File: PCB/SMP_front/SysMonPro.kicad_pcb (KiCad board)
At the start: 2 copper layers, 100 x 100 mm, 0 parts

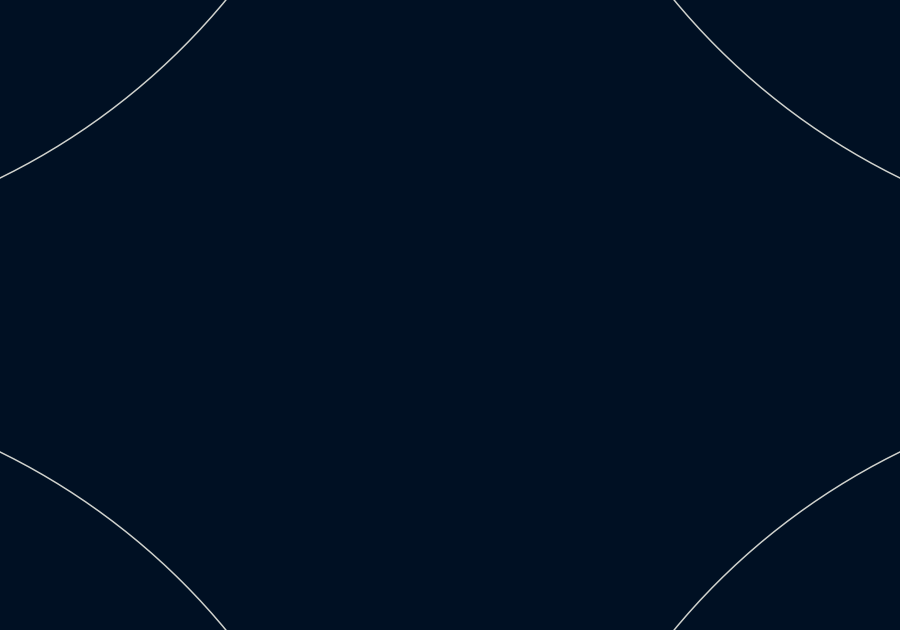
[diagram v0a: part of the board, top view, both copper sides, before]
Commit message: enlarged hole
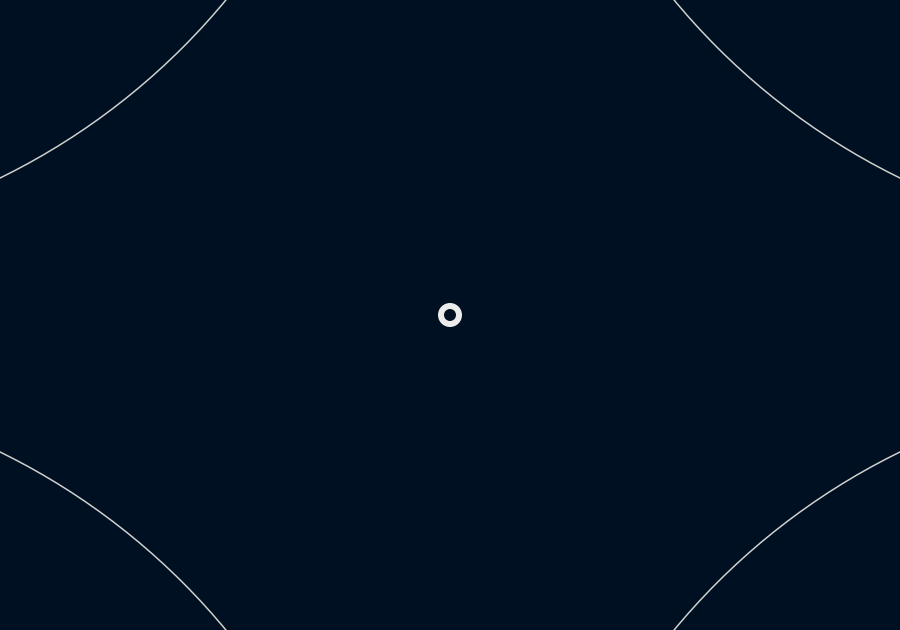
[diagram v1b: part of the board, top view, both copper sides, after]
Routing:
- net (no net): vias 0 -> 1
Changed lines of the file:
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@@
     (effects (font (size 1.5 1) (thickness 0.15)))
   )
+  (via (at 110 110) (size 0.8) (drill 0.4) (layers "F.Cu" "B.Cu") (free) (net 0))
   (zone (net 0) (net_name "") (layer "F.Cu") (hatch edge 0.508)
     (connect_pads (clearance 0.508))
